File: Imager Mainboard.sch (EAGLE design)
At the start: 45 parts, among them IC1 7805H, IC2 MAX3490, IC3 SC16IS740IPW, IC4 MAX3490, IC6 AD7714R-24, J1 RASPBERRYPI-40-PIN-GPIO_PTH_N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, J14 U.FL, Q1 ASFL1, Q2 1.8432 MHz

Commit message: Adding test pads
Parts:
- added TP10, TP11, TP12, TP13, TP8, TP9: PTR1PAD1-13, testpad:PTR1PAD1-13
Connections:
- new net N$21: TP8.TP, U$1.PSCMP
- new net N$25: TP9.TP, U$1.!INT
- new net N$26: TP10.TP, U$1.5V
- new net N$27: Q1.OE, TP11.TP
- new net N$28: DRV2.VREF, TP12.TP
- new net N$29: DRV1.VREF, TP13.TP
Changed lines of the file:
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@@
 <part name="TP6" library="testpad" deviceset="PTR1" device="B1,27" value="PTR1B1,27"/>
 <part name="TP7" library="testpad" deviceset="PTR1" device="B1,27" value="PTR1B1,27"/>
+<part name="TP8" library="testpad" deviceset="PTR1" device="PAD1-13"/>
+<part name="TP9" library="testpad" deviceset="PTR1" device="PAD1-13"/>
+<part name="TP10" library="testpad" deviceset="PTR1" device="PAD1-13"/>
+<part name="TP11" library="testpad" deviceset="PTR1" device="PAD1-13"/>
+<part name="TP12" library="testpad" deviceset="PTR1" device="PAD1-13"/>
+<part name="TP13" library="testpad" deviceset="PTR1" device="PAD1-13"/>
 </parts>
 <sheets>
@@
 <instance part="TP6" gate="G$1" x="-142.24" y="-45.72" rot="R270"/>
 <instance part="TP7" gate="G$1" x="58.42" y="-93.98" rot="R180"/>
+<instance part="TP8" gate="G$1" x="91.44" y="142.24" rot="R270"/>
+<instance part="TP9" gate="G$1" x="91.44" y="137.16" rot="R270"/>
+<instance part="TP10" gate="G$1" x="106.68" y="177.8" rot="R180"/>
+<instance part="TP11" gate="G$1" x="73.66" y="170.18" rot="R180"/>
+<instance part="TP12" gate="G$1" x="132.08" y="78.74" rot="R90"/>
+<instance part="TP13" gate="G$1" x="132.08" y="22.86" rot="R90"/>
 </instances>
 <busses>
@@
 </segment>
 </net>
+<net name="N$21" class="0">
+<segment>
+<pinref part="U$1" gate="G$1" pin="PSCMP"/>
+<pinref part="TP8" gate="G$1" pin="TP"/>
+</segment>
+</net>
+<net name="N$25" class="0">
+<segment>
+<pinref part="U$1" gate="G$1" pin="!INT"/>
+<pinref part="TP9" gate="G$1" pin="TP"/>
+</segment>
+</net>
+<net name="N$26" class="0">
+<segment>
+<pinref part="U$1" gate="G$1" pin="5V"/>
+<pinref part="TP10" gate="G$1" pin="TP"/>
+</segment>
+</net>
+<net name="N$27" class="0">
+<segment>
+<pinref part="Q1" gate="G$1" pin="OE"/>
+<pinref part="TP11" gate="G$1" pin="TP"/>
+</segment>
+</net>
+<net name="N$28" class="0">
+<segment>
+<pinref part="DRV2" gate="G$1" pin="VREF"/>
+<pinref part="TP12" gate="G$1" pin="TP"/>
+</segment>
+</net>
+<net name="N$29" class="0">
+<segment>
+<pinref part="DRV1" gate="G$1" pin="VREF"/>
+<pinref part="TP13" gate="G$1" pin="TP"/>
+</segment>
+</net>

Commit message: Adding TMC429 CS
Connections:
- removed net N$31: U$1.!CS
- new net CS3: J1.GP21, U$1.!CS
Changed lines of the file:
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@@
 </segment>
 </net>
-<net name="N$31" class="0">
+<net name="CS3" class="0">
 <segment>
 <pinref part="U$1" gate="G$1" pin="!CS"/>
@@
 <label x="88.9" y="154.94" size="1.778" layer="95" rot="R180"/>
 </segment>
+<segment>
+<pinref part="J1" gate="G$1" pin="GP21"/>
+<wire x1="12.7" y1="43.18" x2="7.62" y2="43.18" width="0.1524" layer="91"/>
+<label x="7.62" y="43.18" size="1.778" layer="95" rot="R180"/>
+</segment>
 </net>

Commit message: Adding serial test points
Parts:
- added TP14, TP15: PTR1PAD1-13, testpad:PTR1PAD1-13
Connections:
- net N$3: now also TP14.TP
- net N$37: now also TP15.TP
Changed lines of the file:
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@@
 <part name="TP12" library="testpad" deviceset="PTR1" device="PAD1-13"/>
 <part name="TP13" library="testpad" deviceset="PTR1" device="PAD1-13"/>
+<part name="TP14" library="testpad" deviceset="PTR1" device="PAD1-13"/>
+<part name="TP15" library="testpad" deviceset="PTR1" device="PAD1-13"/>
 </parts>
 <sheets>
@@
 <instance part="TP12" gate="G$1" x="132.08" y="78.74" rot="R90"/>
 <instance part="TP13" gate="G$1" x="132.08" y="22.86" rot="R90"/>
+<instance part="TP14" gate="G$1" x="127" y="-78.74" rot="R180"/>
+<instance part="TP15" gate="G$1" x="129.54" y="-81.28" rot="R180"/>
 </instances>
 <busses>
@@
 <pinref part="TP2" gate="G$1" pin="TP"/>
 <wire x1="-15.24" y1="68.58" x2="-17.78" y2="68.58" width="0.1524" layer="91"/>
+<label x="-17.78" y="68.58" size="1.778" layer="95" rot="R180"/>
 </segment>
 </net>
@@
 <pinref part="TP3" gate="G$1" pin="TP"/>
 <wire x1="-15.24" y1="63.5" x2="-17.78" y2="63.5" width="0.1524" layer="91"/>
+<label x="-17.78" y="63.5" size="1.778" layer="95" rot="R180"/>
 </segment>
 </net>
@@
 <pinref part="TP1" gate="G$1" pin="TP"/>
 <wire x1="-15.24" y1="73.66" x2="-17.78" y2="73.66" width="0.1524" layer="91"/>
+<label x="-17.78" y="73.66" size="1.778" layer="95" rot="R180"/>
 </segment>
 </net>
@@
 <pinref part="IC3" gate="G$1" pin="TX"/>
 <pinref part="IC4" gate="G$1" pin="DI"/>
-<wire x1="121.92" y1="-81.28" x2="134.62" y2="-81.28" width="0.1524" layer="91"/>
+<wire x1="121.92" y1="-81.28" x2="127" y2="-81.28" width="0.1524" layer="91"/>
+<wire x1="127" y1="-81.28" x2="134.62" y2="-81.28" width="0.1524" layer="91"/>
 <wire x1="134.62" y1="-81.28" x2="134.62" y2="-77.47" width="0.1524" layer="91"/>
+<pinref part="TP14" gate="G$1" pin="TP"/>
+<junction x="127" y="-81.28"/>
 </segment>
 </net>
@@
 <segment>
 <pinref part="IC3" gate="G$1" pin="RX"/>
-<wire x1="121.92" y1="-83.82" x2="134.62" y2="-83.82" width="0.1524" layer="91"/>
+<wire x1="121.92" y1="-83.82" x2="129.54" y2="-83.82" width="0.1524" layer="91"/>
 <pinref part="IC4" gate="G$1" pin="RO"/>
+<wire x1="129.54" y1="-83.82" x2="134.62" y2="-83.82" width="0.1524" layer="91"/>
 <wire x1="134.62" y1="-83.82" x2="134.62" y2="-87.63" width="0.1524" layer="91"/>
-</segment>
-</net>
+<pinref part="TP15" gate="G$1" pin="TP"/>
+<junction x="129.54" y="-83.82"/>
+</segment>
+</net>

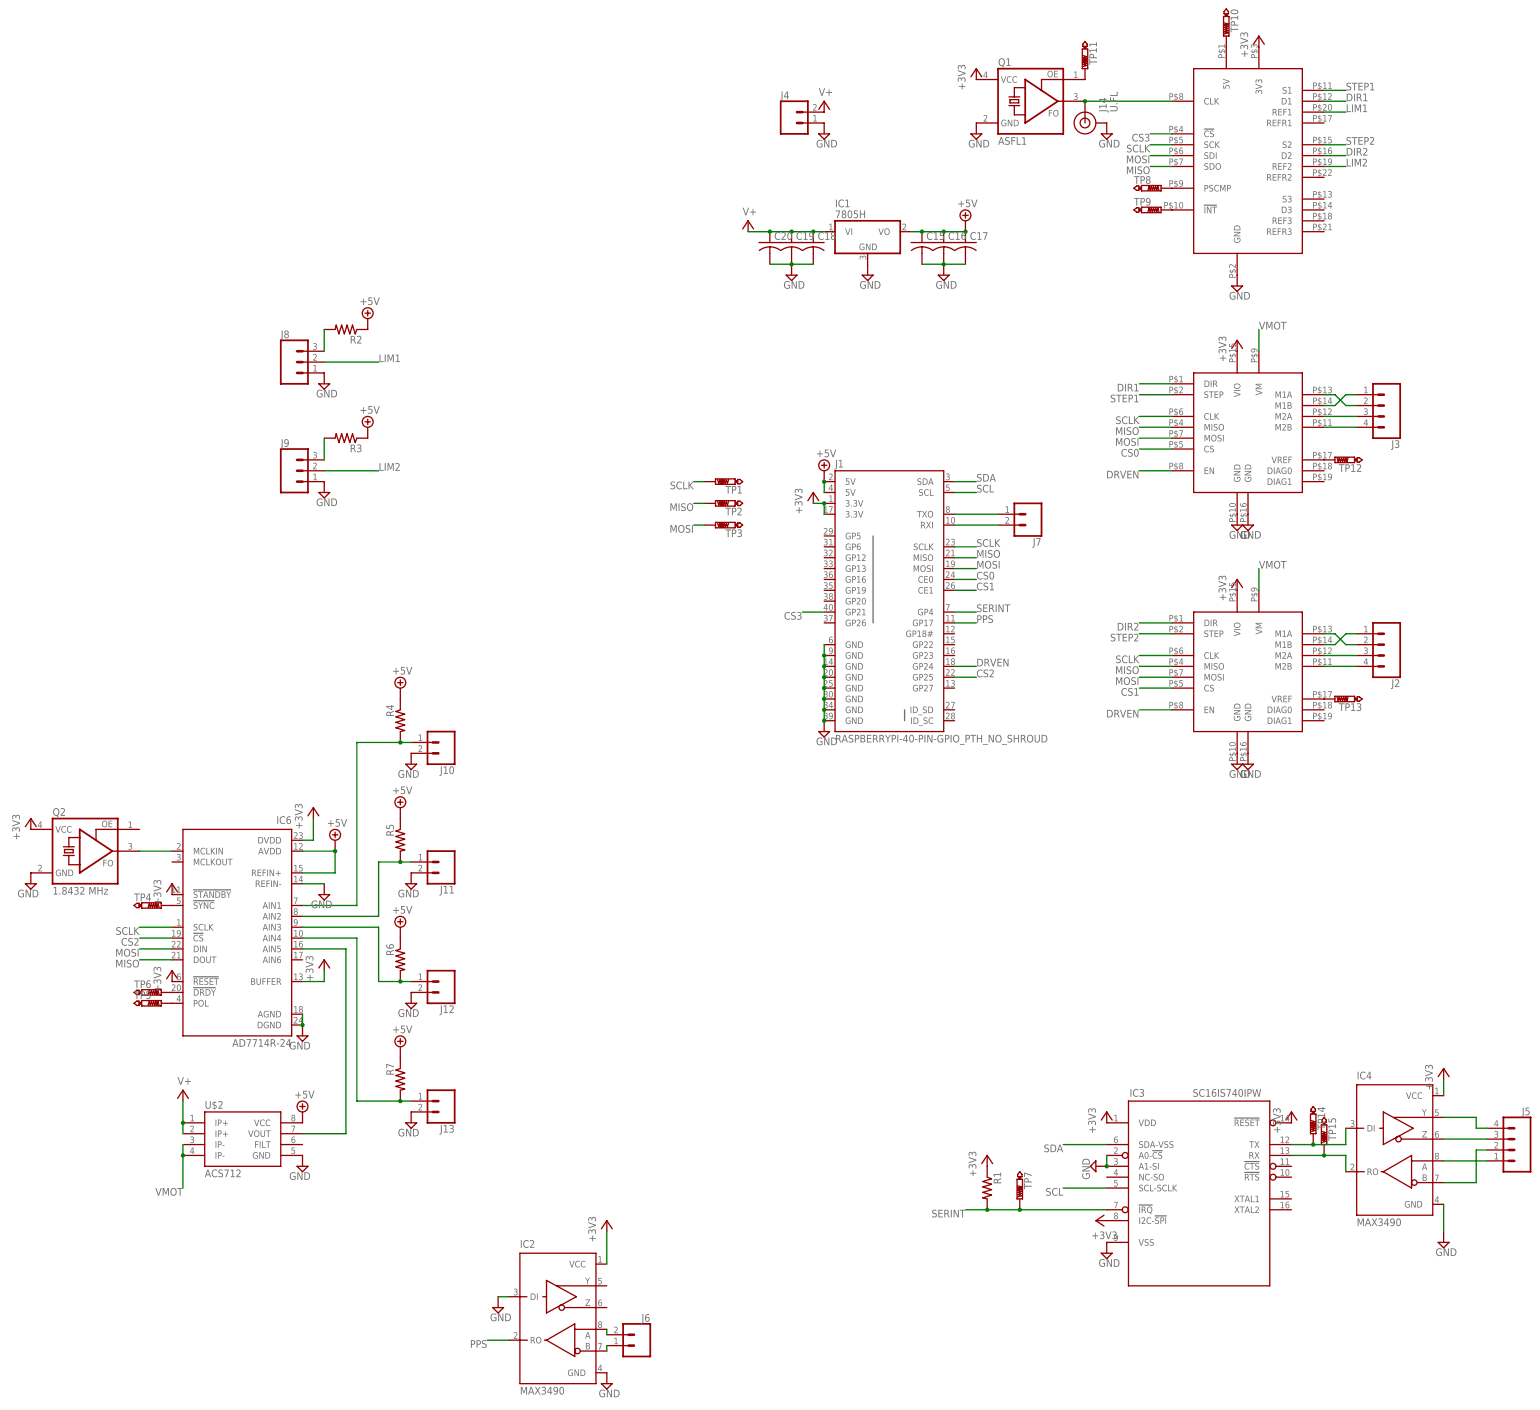
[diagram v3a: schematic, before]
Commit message: Adding SC16IS740 oscillator section and limit switch pullups
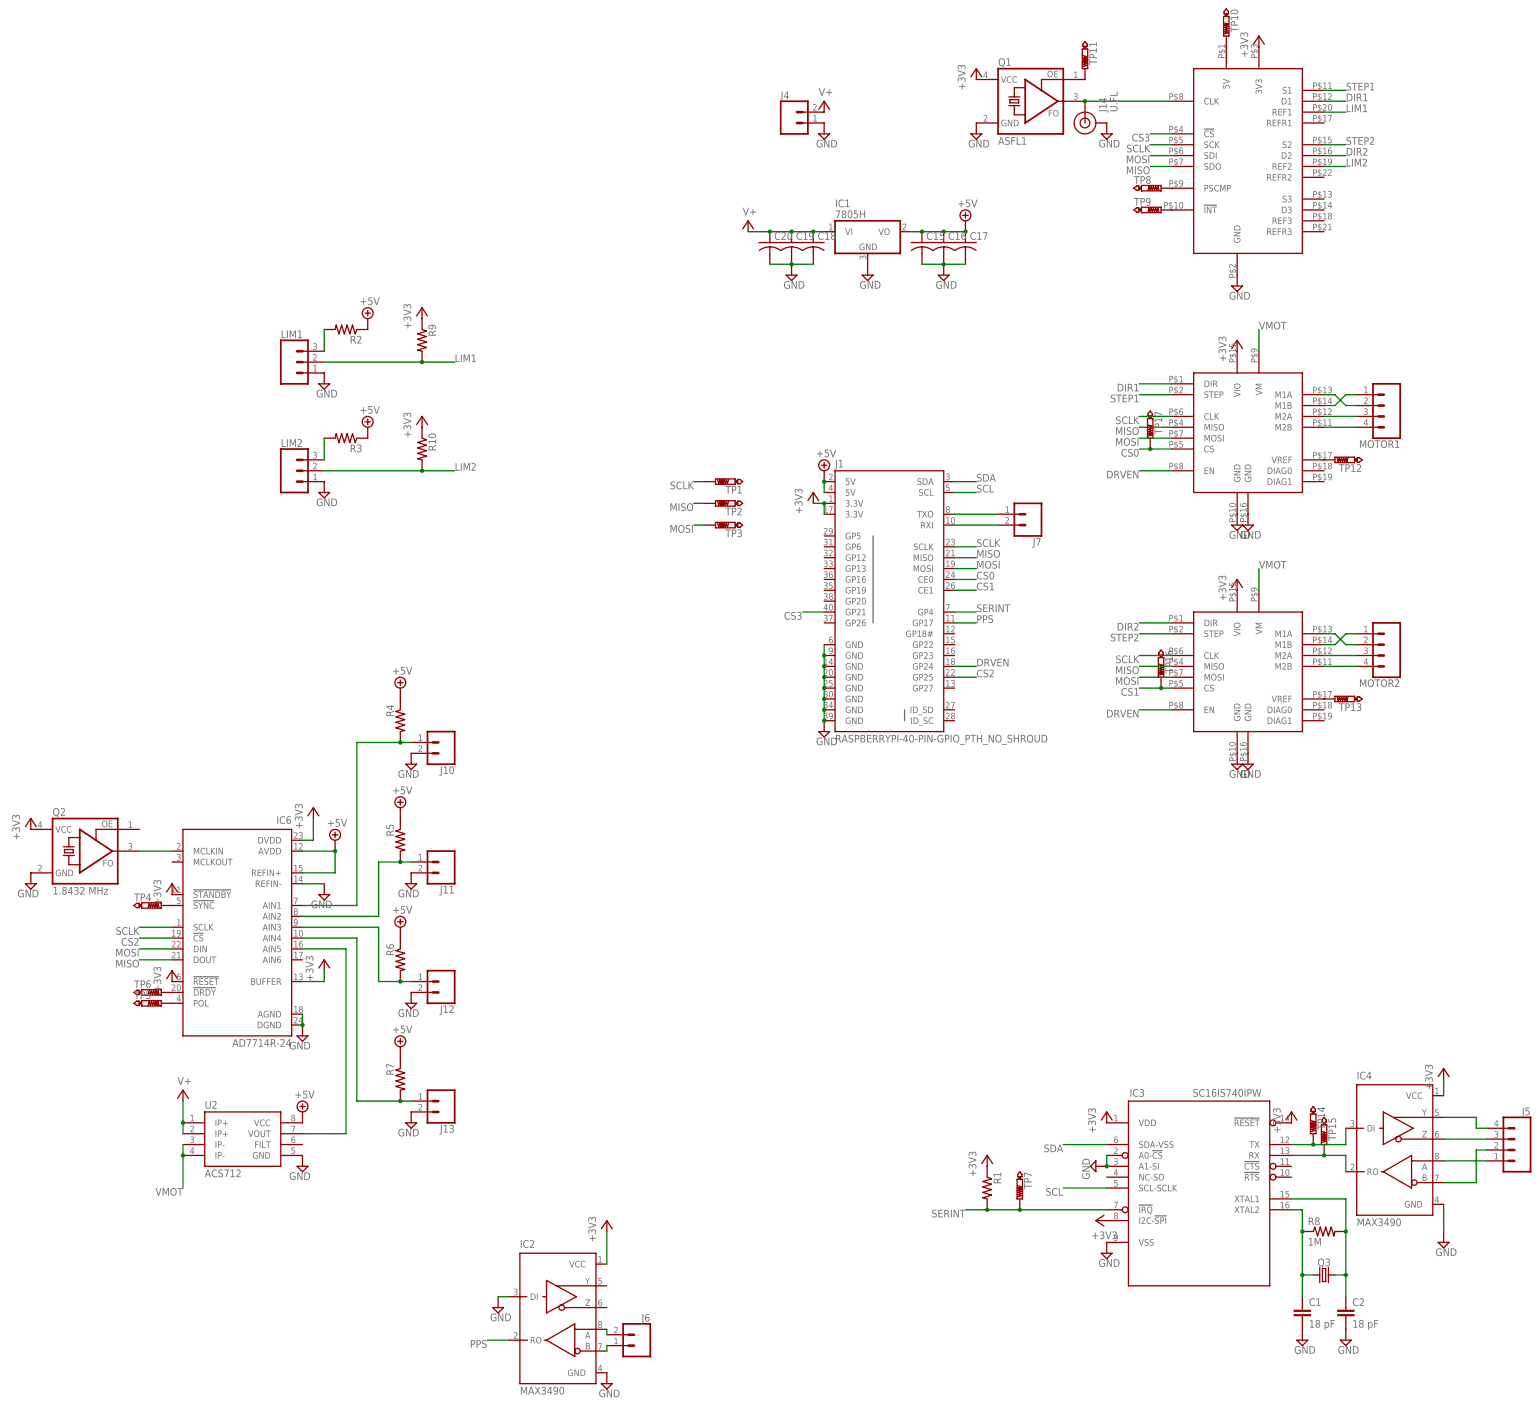
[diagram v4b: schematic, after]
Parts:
- added C1, C2: 18 pF, resistor:C-EUC1206
- added Q3: (no value), SparkFun-Clocks:CRYSTALSMD-5X3.2-4PAD
- added R10, R9: (no value), resistor:R-US_R1206
- added R8: 1M, resistor:R-US_R1206
- added TP16, TP17: PTR1PAD1-13, testpad:PTR1PAD1-13
- renumbered J2 to MOTOR2, J3 to MOTOR1, J8 to LIM1, J9 to LIM2, U$2 to U2
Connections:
- new net N$30: C2.1, IC3.XTAL1, Q3.2, R8.2
- new net N$31: C1.1, IC3.XTAL2, Q3.1, R8.1
- net +3V3: now also R10.1, R9.1
- net CS0: now also DRV1.CS, TP17.TP; no longer DRV2.CS
- net CS1: now also DRV2.CS, TP16.TP; no longer DRV1.CS
- net DIR1: now also DRV1.DIR; no longer DRV2.DIR
- net DIR2: now also DRV2.DIR; no longer DRV1.DIR
- net GND: now also C1.2, C2.2
- net LIM1: now also R9.2
- net LIM2: now also R10.2
- net N$1: now also DRV2.M1B; no longer DRV1.M1B
- net N$2: now also DRV2.M1A; no longer DRV1.M1A
- net N$28: now also DRV1.VREF; no longer DRV2.VREF
- net N$29: now also DRV2.VREF; no longer DRV1.VREF
- net N$4: now also DRV2.M2A; no longer DRV1.M2A
- net N$5: now also DRV2.M2B; no longer DRV1.M2B
- net N$6: now also DRV1.M1B; no longer DRV2.M1B
- net N$7: now also DRV1.M1A; no longer DRV2.M1A
- net N$8: now also DRV1.M2A; no longer DRV2.M2A
- net N$9: now also DRV1.M2B; no longer DRV2.M2B
- net STEP1: now also DRV1.STEP; no longer DRV2.STEP
- net STEP2: now also DRV2.STEP; no longer DRV1.STEP
